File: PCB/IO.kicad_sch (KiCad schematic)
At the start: 39 parts, among them J501 Conn_02x03_Counter_Clockwise, J502 USB_C_Receptacle_USB2.0_16P, J503 Screw_Terminal_01x06, J504 Screw_Terminal_01x04, J505 Conn_01x04, J506 Conn_02x03_Counter_Clockwise, J507 Conn_01x06, J508 VCC, Q1 SL2302S, SW1 SW_Push, SW2 SW_Push

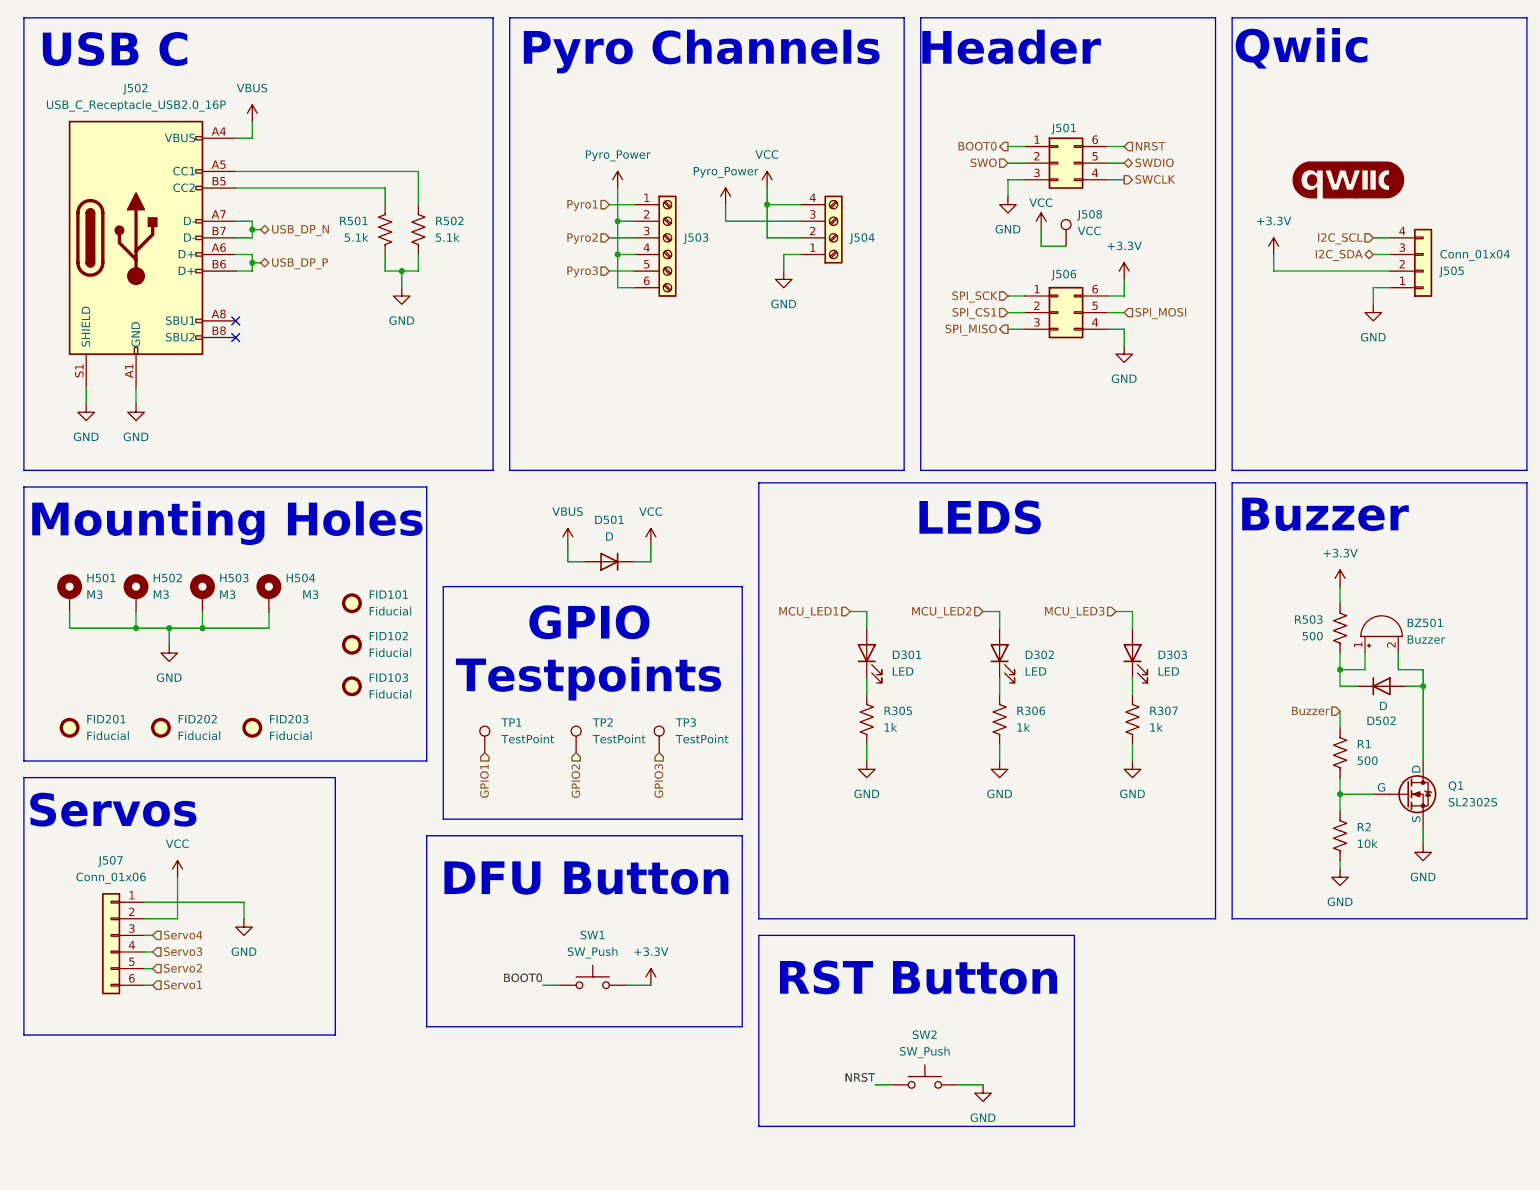
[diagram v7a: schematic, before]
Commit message: Replaced the radio in the schematic
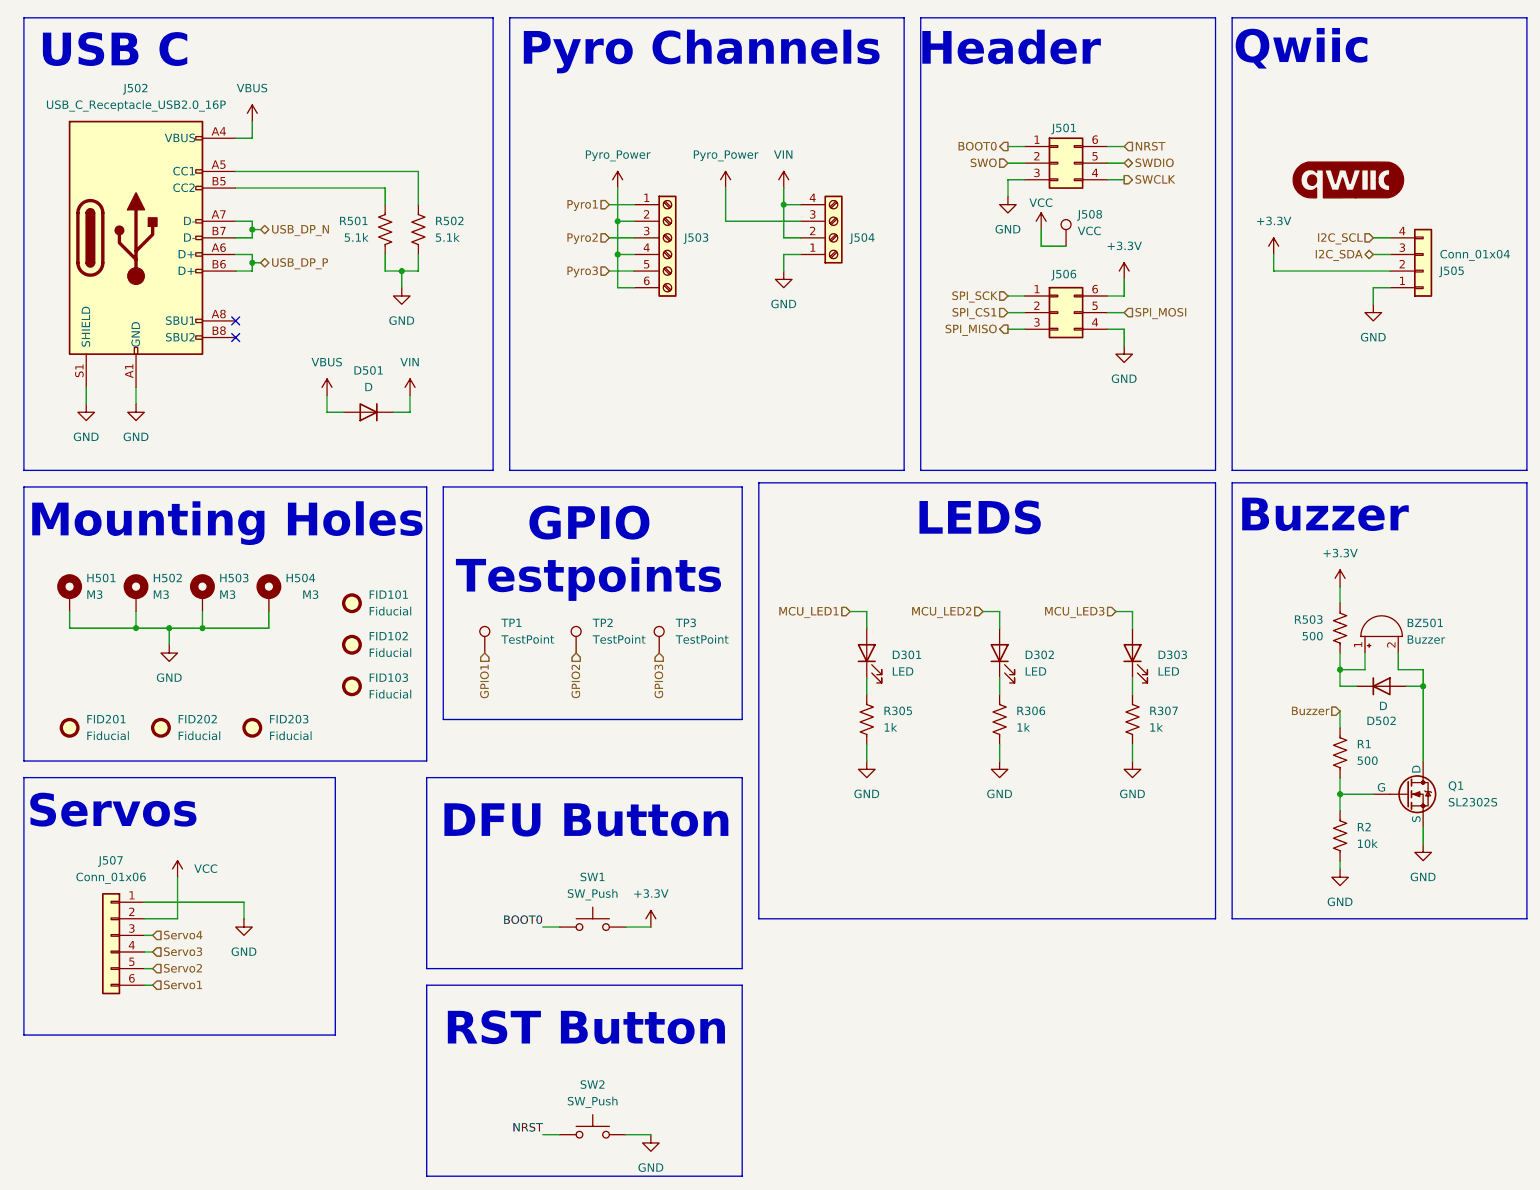
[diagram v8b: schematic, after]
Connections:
- net VCC: no longer D501.3 (K), J504.2 (Pin_2), J504.4 (Pin_4)
- new net VIN: D501.3 (K), J504.2 (Pin_2), J504.4 (Pin_4)
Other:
- moved on the sheet: D501, SW1, SW2, TP1, TP2, TP3
